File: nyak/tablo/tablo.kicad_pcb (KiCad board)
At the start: 2 copper layers, 163.8 x 106.7 mm, 110 parts

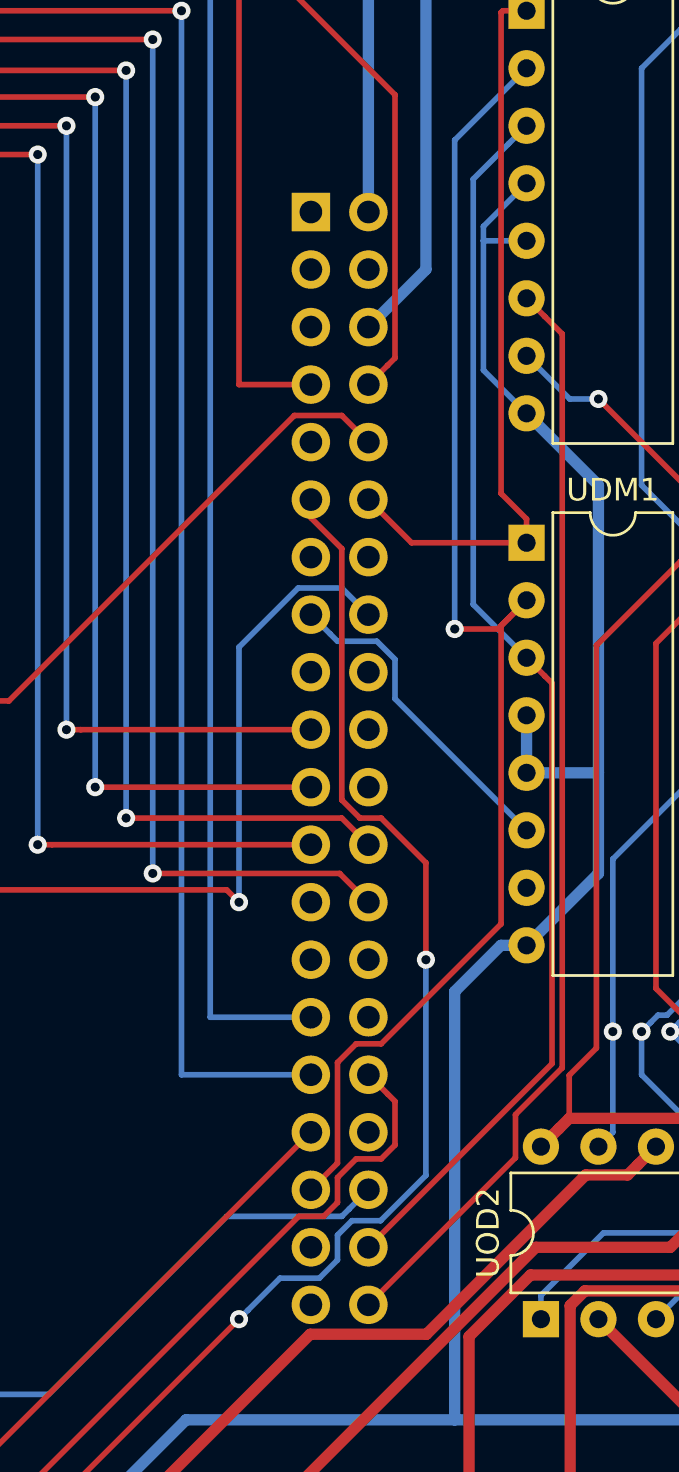
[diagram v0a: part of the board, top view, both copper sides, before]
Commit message: updated rpi gpio connector footprint
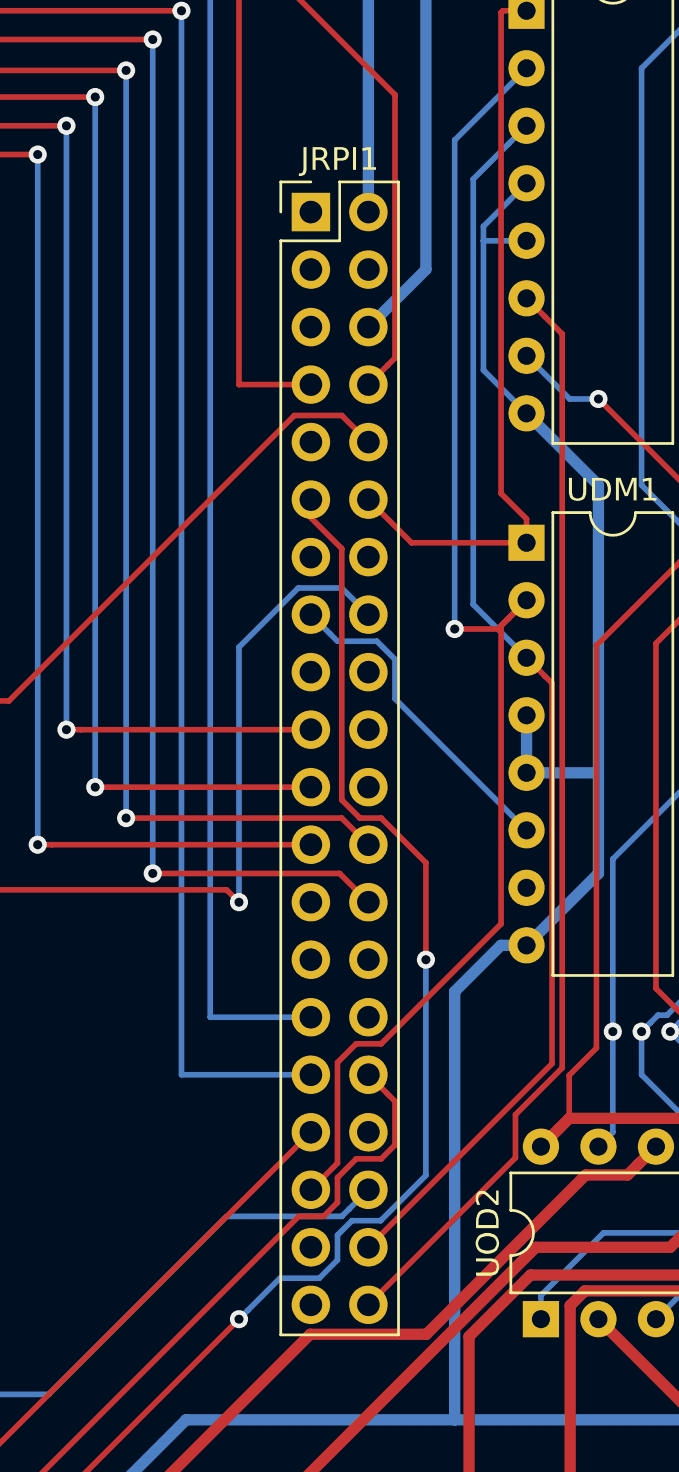
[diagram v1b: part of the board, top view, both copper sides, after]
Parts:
- JRPI1: footprint Connector_PinSocket_2.54mm:PinSocket_2x20_P2.54mm_Vertical -> Connector_PinHeader_2.54mm:PinHeader_2x20_P2.54mm_Vertical; moved to F.Cu
- turned JRPI1 to 0 degrees

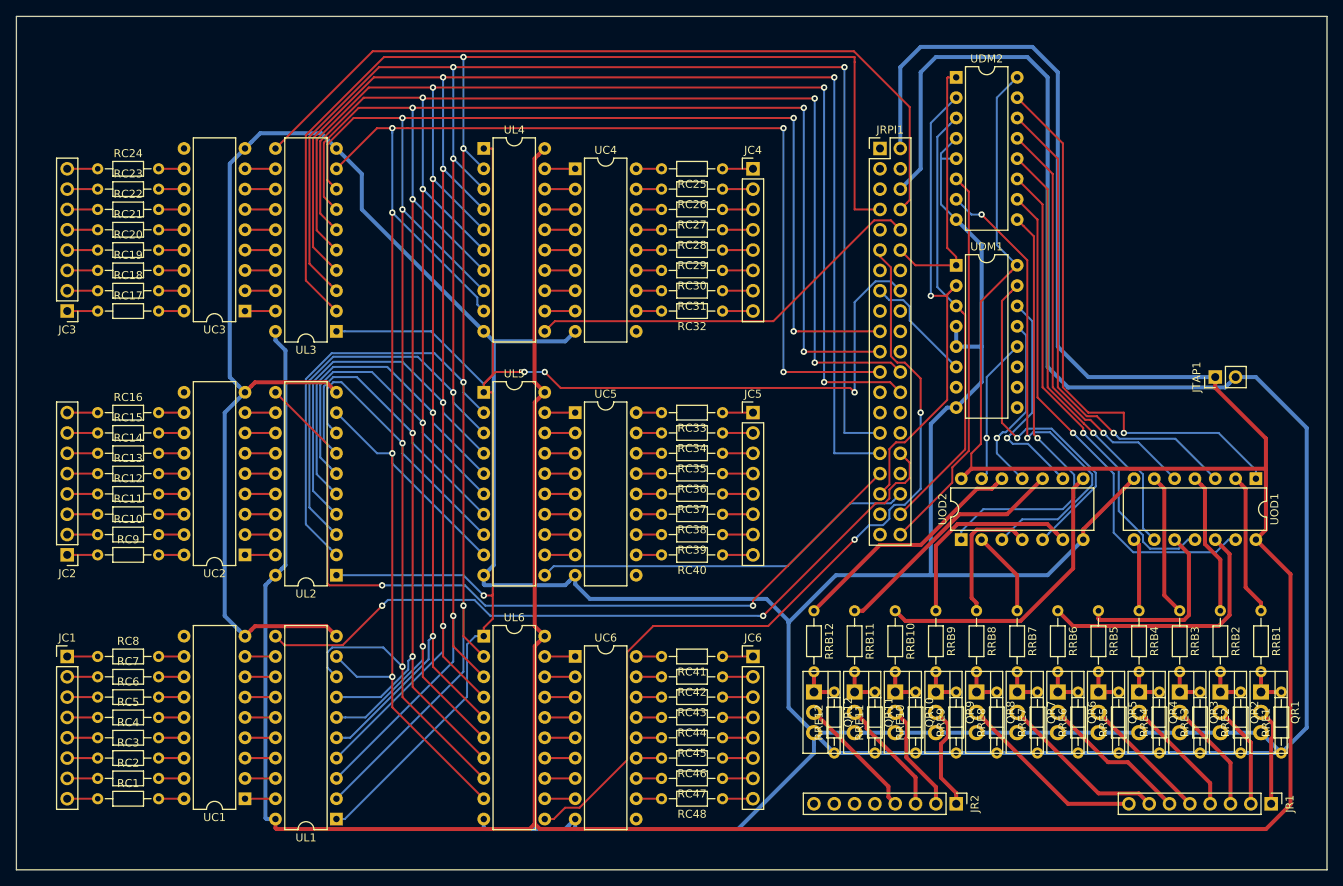
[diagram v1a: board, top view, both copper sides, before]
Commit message: Fixed row switch PNP transistor emitter connection from GND to VCC
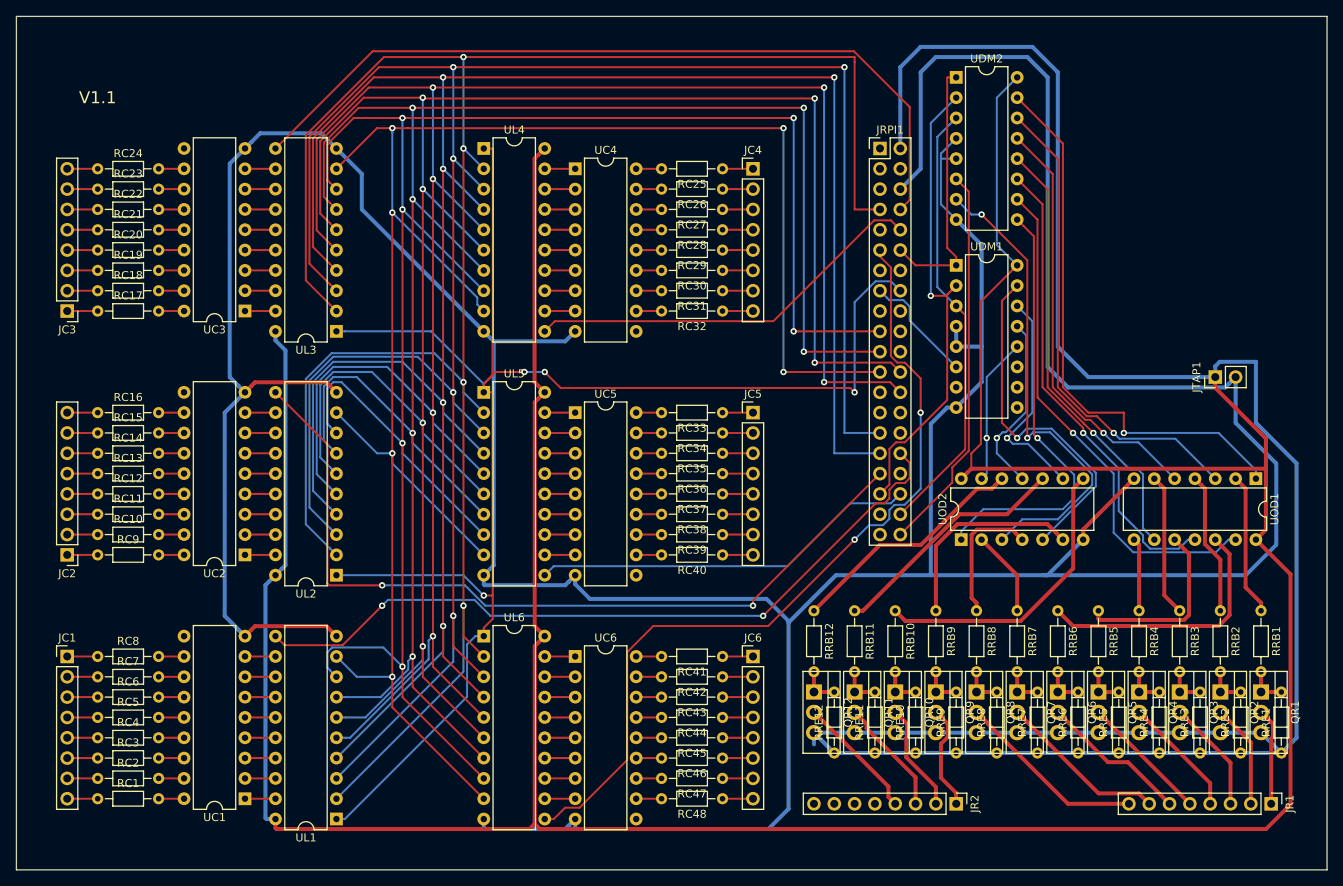
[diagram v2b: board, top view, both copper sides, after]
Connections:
- QR1 pad 3: Earth -> VCC
- QR10 pad 3: Earth -> VCC
- QR11 pad 3: Earth -> VCC
- QR12 pad 3: Earth -> VCC
- QR2 pad 3: Earth -> VCC
- QR3 pad 3: Earth -> VCC
- QR4 pad 3: Earth -> VCC
- QR5 pad 3: Earth -> VCC
- QR6 pad 3: Earth -> VCC
- QR7 pad 3: Earth -> VCC
- QR8 pad 3: Earth -> VCC
- QR9 pad 3: Earth -> VCC
- RRE1 pad 1: Earth -> VCC
- RRE10 pad 1: Earth -> VCC
- RRE11 pad 1: Earth -> VCC
- RRE12 pad 1: Earth -> VCC
- RRE2 pad 1: Earth -> VCC
- RRE3 pad 1: Earth -> VCC
- RRE4 pad 1: Earth -> VCC
- RRE5 pad 1: Earth -> VCC
- RRE6 pad 1: Earth -> VCC
- RRE7 pad 1: Earth -> VCC
- RRE8 pad 1: Earth -> VCC
- RRE9 pad 1: Earth -> VCC
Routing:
- net VCC: track 518.7 -> 698.3 mm
- net Earth: track 671.6 -> 551.9 mm
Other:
- board text added: "V1.1"

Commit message: Updated resistor footprints to have 0.8mm holes instead of 0.7
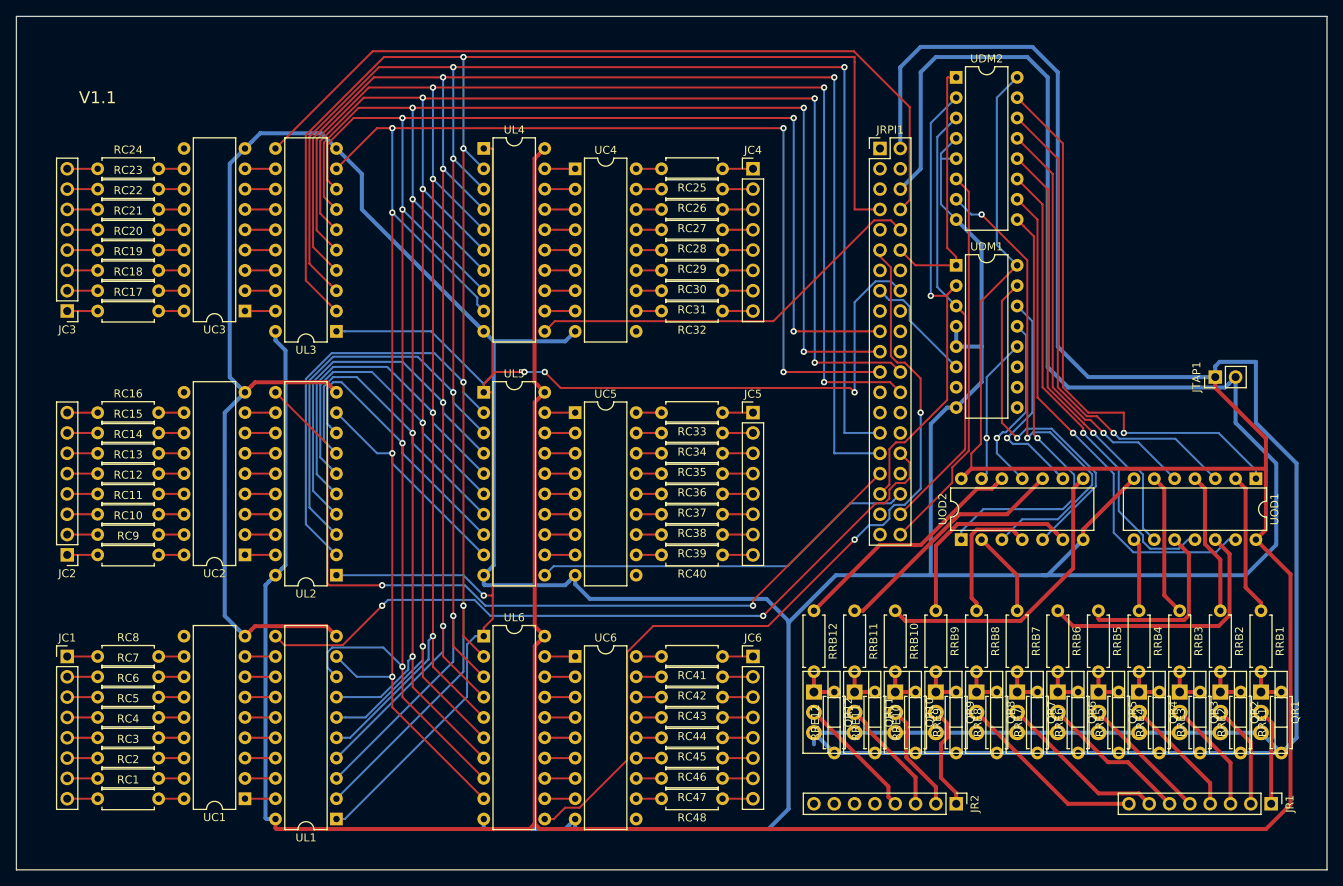
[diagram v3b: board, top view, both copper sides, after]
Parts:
- RC1, RC10, RC11, RC12, RC13, RC14, RC15, RC16, RC17, RC18, RC19, RC2, RC20, RC21, RC22, RC23, RC24, RC25, RC26, RC27, RC28, RC29, RC3, RC30, RC31, RC32, RC33, RC34, RC35, RC36, RC37, RC38, RC39, RC4, RC40, RC41, RC42, RC43, RC44, RC45, RC46, RC47, RC48, RC5, RC6, RC7, RC8, RC9, RRB1, RRB10, RRB11, RRB12, RRB2, RRB3, RRB4, RRB5, RRB6, RRB7, RRB8, RRB9, RRE1, RRE10, RRE11, RRE12, RRE2, RRE3, RRE4, RRE5, RRE6, RRE7, RRE8, RRE9: footprint Resistor_THT:R_Axial_DIN0204_L3.6mm_D1.6mm_P7.62mm_Horizontal -> Resistor_THT:R_Axial_DIN0207_L6.3mm_D2.5mm_P7.62mm_Horizontal
